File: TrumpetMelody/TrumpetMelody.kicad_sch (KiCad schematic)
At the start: 81 parts, among them J1 USB_B_Micro, J2 Conn_01x05, J3 640456-3, J4 640456-3, SW1 SW_Push, U1 STM32F411RETx, U2 TLV62565DBVR, U3 MAX98357AETE_T, U4 MAX7375AXR805

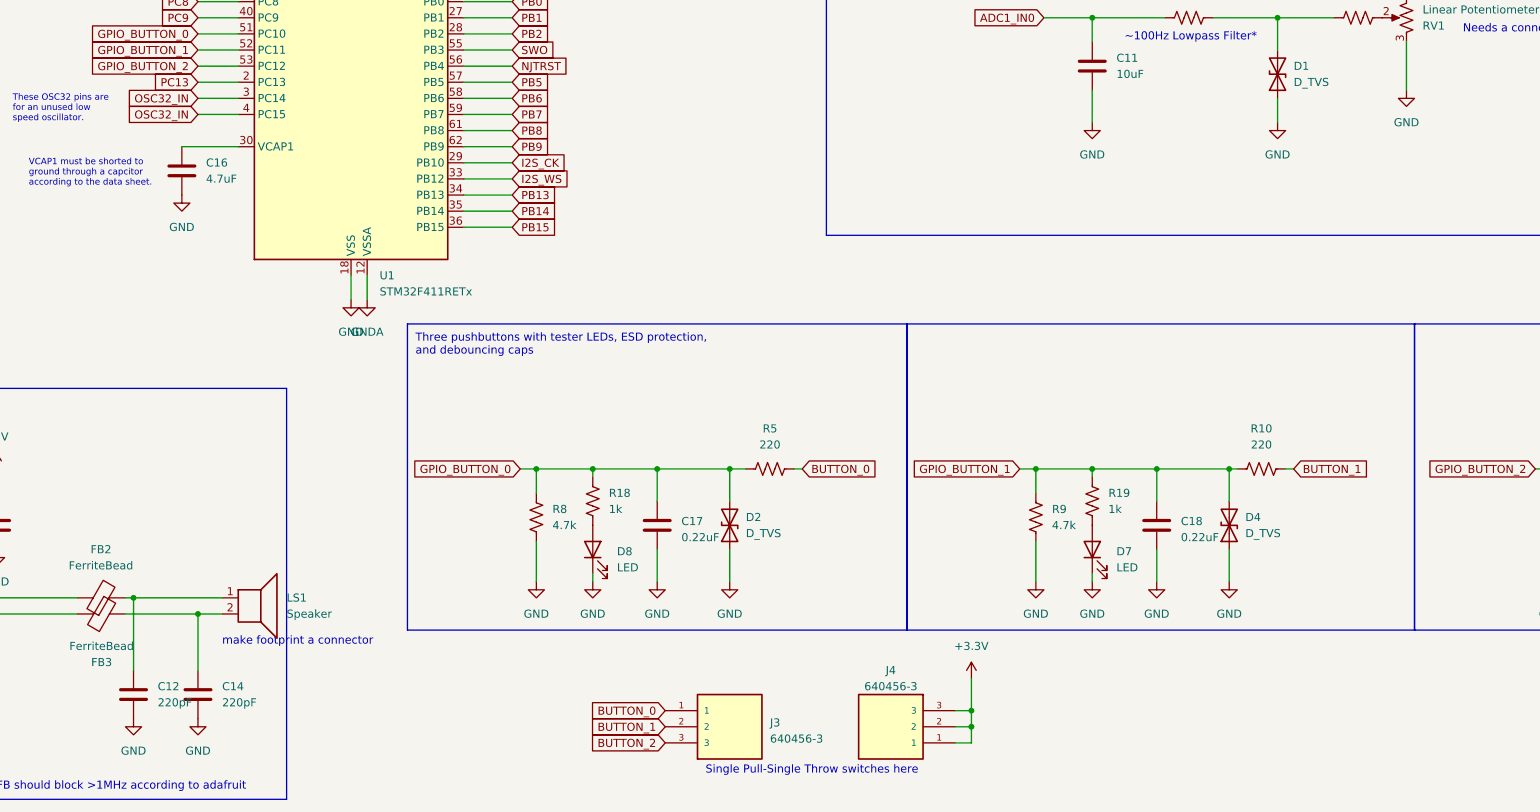
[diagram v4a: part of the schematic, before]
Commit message: Fixed grounds on the speaker and potentiometer
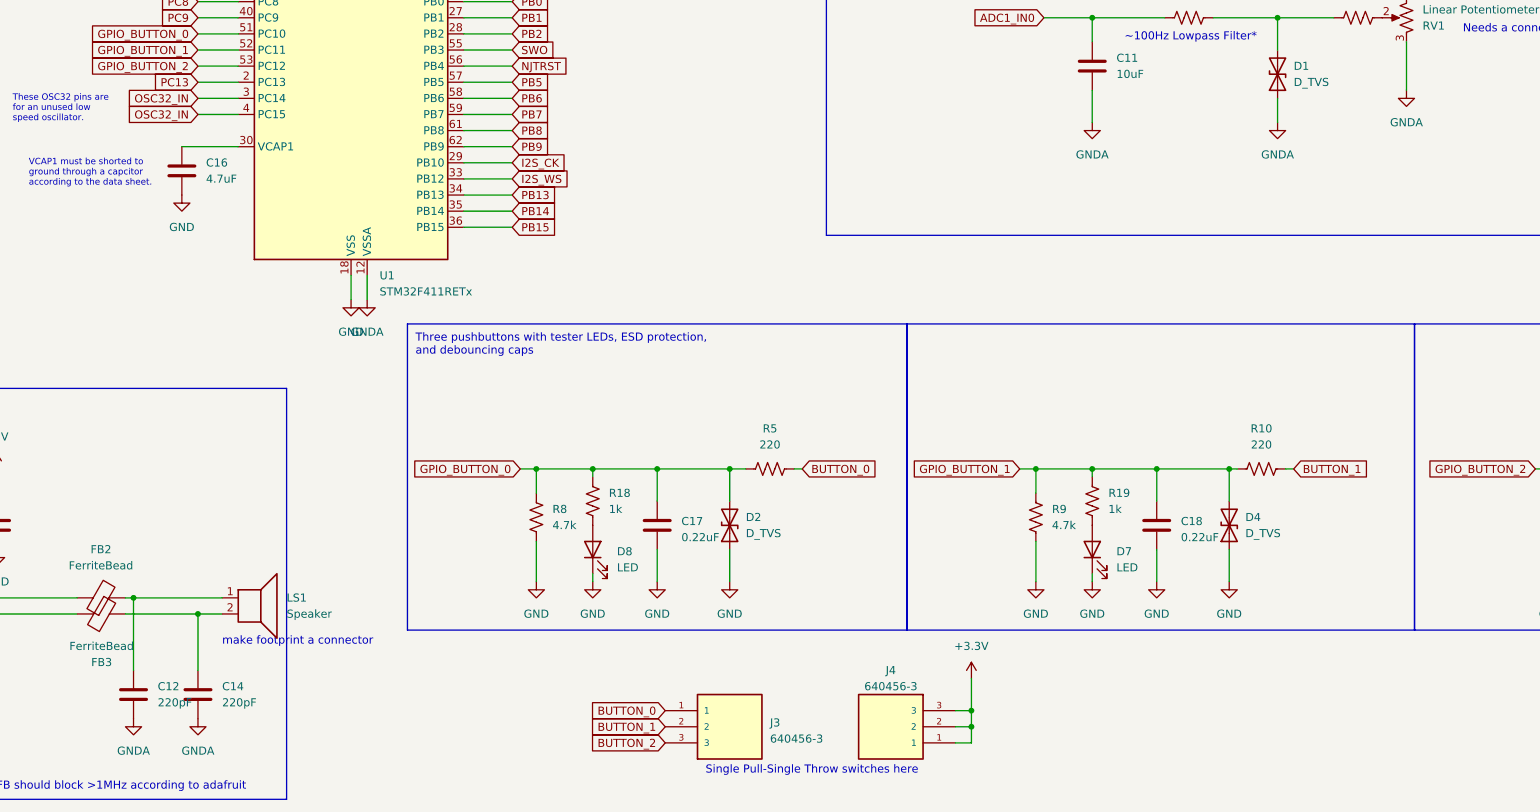
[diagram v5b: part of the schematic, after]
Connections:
- net GND: no longer C11.2, C12.2, C14.2, D1.1 (A1), RV1.3
- net GNDA: now also C11.2, C12.2, C14.2, D1.1 (A1), RV1.3
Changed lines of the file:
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@@
-    )
-  )
-  (symbol (lib_id "power:GND") (at 132.08 261.62 0) (unit 1)
-    (in_bom yes) (on_board yes) (dnp no) (fields_autoplaced)
-    (property "Reference" "#PWR037" (at 132.08 267.97 0)
-      (effects (font (size 1.27 1.27)) hide)
-    )
-    (property "Value" "GND" (at 132.08 266.7 0)
-      (effects (font (size 1.27 1.27)))
-    )
-    (property "Footprint" "" (at 132.08 261.62 0)
-      (effects (font (size 1.27 1.27)) hide)
-    )
-    (property "Datasheet" "" (at 132.08 261.62 0)
-      (effects (font (size 1.27 1.27)) hide)
-    )
-    (pin "1")
-    (instances
-      (project "TrumpetMelody"
-        (path "/646bb87a-580f-408c-a344-dec391089cbb"
-          (reference "#PWR037") (unit 1)
-        )
-      )
     )
   )
@@
     )
   )
+  (symbol (lib_id "power:GNDA") (at 322.58 162.56 0) (unit 1)
+    (in_bom yes) (on_board yes) (dnp no) (fields_autoplaced)
+    (property "Reference" "#PWR018" (at 322.58 168.91 0)
+      (effects (font (size 1.27 1.27)) hide)
+    )
+    (property "Value" "GNDA" (at 322.58 167.64 0)
+      (effects (font (size 1.27 1.27)))
+    )
+    (property "Footprint" "" (at 322.58 162.56 0)
+      (effects (font (size 1.27 1.27)) hide)
+    )
+    (property "Datasheet" "" (at 322.58 162.56 0)
+      (effects (font (size 1.27 1.27)) hide)
+    )
+    (pin "1")
+    (instances
+      (project "TrumpetMelody"
+        (path "/646bb87a-580f-408c-a344-dec391089cbb"
+          (reference "#PWR018") (unit 1)
+        )
+      )
+    )
+  )
   (symbol (lib_id "Device:R_US") (at 257.81 95.25 90) (unit 1)
     (in_bom yes) (on_board yes) (dnp no) (fields_autoplaced)
@@
     )
   )
+  (symbol (lib_id "power:GNDA") (at 121.92 261.62 0) (unit 1)
+    (in_bom yes) (on_board yes) (dnp no) (fields_autoplaced)
+    (property "Reference" "#PWR033" (at 121.92 267.97 0)
+      (effects (font (size 1.27 1.27)) hide)
+    )
+    (property "Value" "GNDA" (at 121.92 266.7 0)
+      (effects (font (size 1.27 1.27)))
+    )
+    (property "Footprint" "" (at 121.92 261.62 0)
+      (effects (font (size 1.27 1.27)) hide)
+    )
+    (property "Datasheet" "" (at 121.92 261.62 0)
+      (effects (font (size 1.27 1.27)) hide)
+    )
+    (pin "1")
+    (instances
+      (project "TrumpetMelody"
+        (path "/646bb87a-580f-408c-a344-dec391089cbb"
+          (reference "#PWR033") (unit 1)
+        )
+      )
+    )
+  )
+  (symbol (lib_id "power:GNDA") (at 302.26 167.64 0) (unit 1)
+    (in_bom yes) (on_board yes) (dnp no) (fields_autoplaced)
+    (property "Reference" "#PWR020" (at 302.26 173.99 0)
+      (effects (font (size 1.27 1.27)) hide)
+    )
+    (property "Value" "GNDA" (at 302.26 172.72 0)
+      (effects (font (size 1.27 1.27)))
+    )
+    (property "Footprint" "" (at 302.26 167.64 0)
+      (effects (font (size 1.27 1.27)) hide)
+    )
+    (property "Datasheet" "" (at 302.26 167.64 0)
+      (effects (font (size 1.27 1.27)) hide)
+    )
+    (pin "1")
+    (instances
+      (project "TrumpetMelody"
+        (path "/646bb87a-580f-408c-a344-dec391089cbb"
+          (reference "#PWR020") (unit 1)
+        )
+      )
+    )
+  )
   (symbol (lib_id "power:+5V") (at 15.24 20.32 0) (unit 1)
     (in_bom yes) (on_board yes) (dnp no) (fields_autoplaced)
@@
         (path "/646bb87a-580f-408c-a344-dec391089cbb"
           (reference "R6") (unit 1)
-        )
-      )
-    )
-  )
-  (symbol (lib_id "power:GND") (at 121.92 261.62 0) (unit 1)
-    (in_bom yes) (on_board yes) (dnp no) (fields_autoplaced)
-    (property "Reference" "#PWR036" (at 121.92 267.97 0)
-      (effects (font (size 1.27 1.27)) hide)
-    )
-    (property "Value" "GND" (at 121.92 266.7 0)
-      (effects (font (size 1.27 1.27)))
-    )
-    (property "Footprint" "" (at 121.92 261.62 0)
-      (effects (font (size 1.27 1.27)) hide)
-    )
-    (property "Datasheet" "" (at 121.92 261.62 0)
-      (effects (font (size 1.27 1.27)) hide)
-    )
-    (pin "1")
-    (instances
-      (project "TrumpetMelody"
-        (path "/646bb87a-580f-408c-a344-dec391089cbb"
-          (reference "#PWR036") (unit 1)
         )
       )
@@
         (path "/646bb87a-580f-408c-a344-dec391089cbb"
           (reference "RV1") (unit 1)
-        )
-      )
-    )
-  )
-  (symbol (lib_id "power:GND") (at 273.05 167.64 0) (unit 1)
-    (in_bom yes) (on_board yes) (dnp no) (fields_autoplaced)
-    (property "Reference" "#PWR021" (at 273.05 173.99 0)
-      (effects (font (size 1.27 1.27)) hide)
-    )
-    (property "Value" "GND" (at 273.05 172.72 0)
-      (effects (font (size 1.27 1.27)))
-    )
-    (property "Footprint" "" (at 273.05 167.64 0)
-      (effects (font (size 1.27 1.27)) hide)
-    )
-    (property "Datasheet" "" (at 273.05 167.64 0)
-      (effects (font (size 1.27 1.27)) hide)
-    )
-    (pin "1")
-    (instances
-      (project "TrumpetMelody"
-        (path "/646bb87a-580f-408c-a344-dec391089cbb"
-          (reference "#PWR021") (unit 1)
         )
       )
@@
     )
   )
-  (symbol (lib_id "power:GND") (at 322.58 162.56 0) (unit 1)
-    (in_bom yes) (on_board yes) (dnp no) (fields_autoplaced)
-    (property "Reference" "#PWR018" (at 322.58 168.91 0)
-      (effects (font (size 1.27 1.27)) hide)
-    )
-    (property "Value" "GND" (at 322.58 167.64 0)
-      (effects (font (size 1.27 1.27)))
-    )
-    (property "Footprint" "" (at 322.58 162.56 0)
-      (effects (font (size 1.27 1.27)) hide)
-    )
-    (property "Datasheet" "" (at 322.58 162.56 0)
-      (effects (font (size 1.27 1.27)) hide)
-    )
-    (pin "1")
-    (instances
-      (project "TrumpetMelody"
-        (path "/646bb87a-580f-408c-a344-dec391089cbb"
-          (reference "#PWR018") (unit 1)
-        )
-      )
-    )
-  )
   (symbol (lib_id "power:GND") (at 30.48 87.63 0) (unit 1)
     (in_bom yes) (on_board yes) (dnp no)
@@
     )
   )
+  (symbol (lib_id "power:GNDA") (at 273.05 167.64 0) (unit 1)
+    (in_bom yes) (on_board yes) (dnp no) (fields_autoplaced)
+    (property "Reference" "#PWR021" (at 273.05 173.99 0)
+      (effects (font (size 1.27 1.27)) hide)
+    )
+    (property "Value" "GNDA" (at 273.05 172.72 0)
+      (effects (font (size 1.27 1.27)))
+    )
+    (property "Footprint" "" (at 273.05 167.64 0)
+      (effects (font (size 1.27 1.27)) hide)
+    )
+    (property "Datasheet" "" (at 273.05 167.64 0)
+      (effects (font (size 1.27 1.27)) hide)
+    )
+    (pin "1")
+    (instances
+      (project "TrumpetMelody"
+        (path "/646bb87a-580f-408c-a344-dec391089cbb"
+          (reference "#PWR021") (unit 1)
+        )
+      )
+    )
+  )
   (symbol (lib_id "Device:C") (at 264.16 35.56 0) (unit 1)
     (in_bom yes) (on_board yes) (dnp no) (fields_autoplaced)
@@
     )
   )
-  (symbol (lib_id "power:GND") (at 302.26 167.64 0) (unit 1)
-    (in_bom yes) (on_board yes) (dnp no) (fields_autoplaced)
-    (property "Reference" "#PWR020" (at 302.26 173.99 0)
-      (effects (font (size 1.27 1.27)) hide)
-    )
-    (property "Value" "GND" (at 302.26 172.72 0)
-      (effects (font (size 1.27 1.27)))
-    )
-    (property "Footprint" "" (at 302.26 167.64 0)
-      (effects (font (size 1.27 1.27)) hide)
-    )
-    (property "Datasheet" "" (at 302.26 167.64 0)
-      (effects (font (size 1.27 1.27)) hide)
-    )
-    (pin "1")
-    (instances
-      (project "TrumpetMelody"
-        (path "/646bb87a-580f-408c-a344-dec391089cbb"
-          (reference "#PWR020") (unit 1)
-        )
-      )
+  (symbol (lib_id "power:GNDA") (at 132.08 261.62 0) (unit 1)
+    (in_bom yes) (on_board yes) (dnp no) (fields_autoplaced)
+    (property "Reference" "#PWR034" (at 132.08 267.97 0)
+      (effects (font (size 1.27 1.27)) hide)
+    )
+    (property "Value" "GNDA" (at 132.08 266.7 0)
+      (effects (font (size 1.27 1.27)))
+    )
+    (property "Footprint" "" (at 132.08 261.62 0)
+      (effects (font (size 1.27 1.27)) hide)
+    )
+    (property "Datasheet" "" (at 132.08 261.62 0)
+      (effects (font (size 1.27 1.27)) hide)
+    )
+    (pin "1")
+    (instances
+      (project "TrumpetMelody"
+        (path "/646bb87a-580f-408c-a344-dec391089cbb"
+          (reference "#PWR034") (unit 1)
+        )
+      )

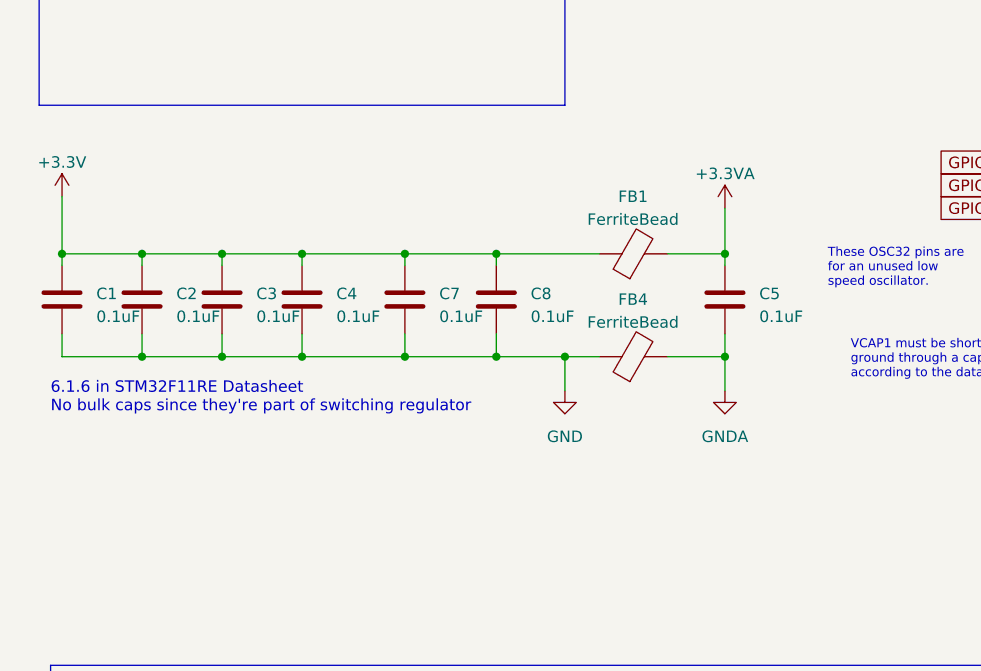
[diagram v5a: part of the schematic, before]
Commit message: Added decoupling caps to the micro
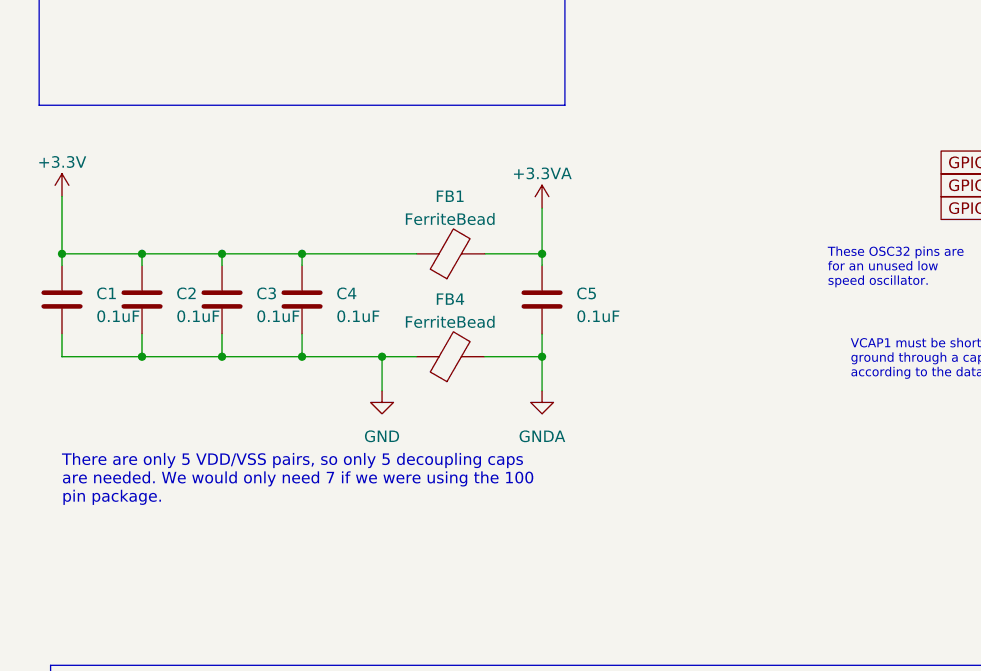
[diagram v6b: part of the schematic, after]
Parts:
- removed C7, C8: 0.1uF, Capacitor_SMD:C_0805_2012Metric_Pad1.18x1.45mm_HandSolder, symbol Device:C
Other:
- note added: "There are only 5 VDD/VSS pairs, so only 5 decoupling caps are needed. We would only need 7 if we were using the 100 pin package."
- note removed: "6.1.6 in STM32F11RE Datasheet No bulk caps since they're part of switching regulator"
- moved on the sheet: C5, FB1, FB4

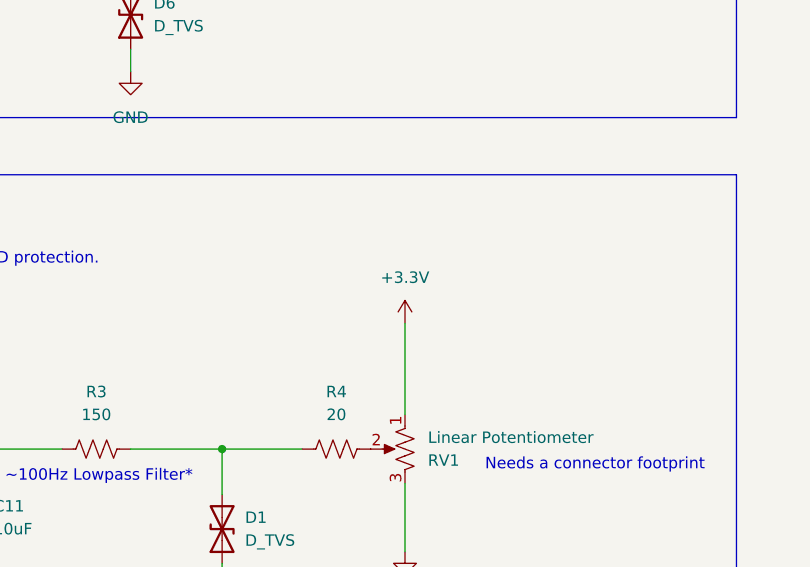
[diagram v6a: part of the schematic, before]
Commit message: Changed +3.3V on the poteniometer to +3.3VA
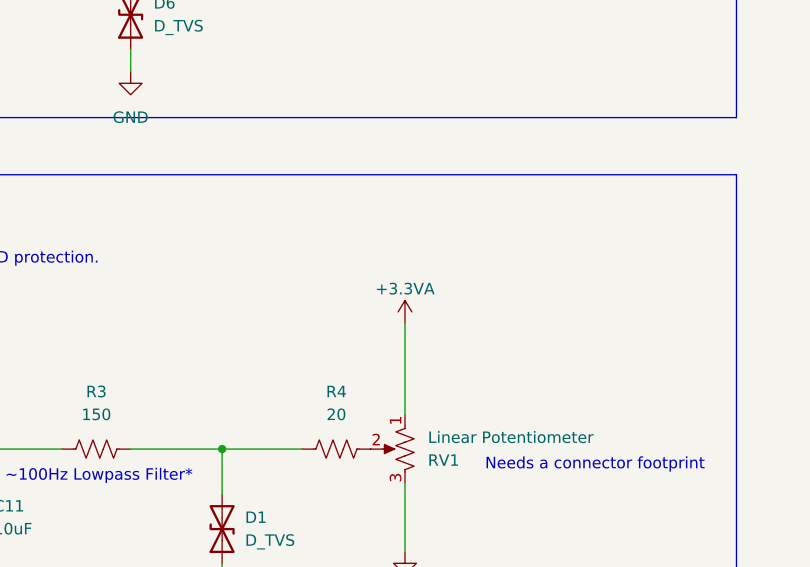
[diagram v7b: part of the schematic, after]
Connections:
- net +3.3V: no longer RV1.1
- net +3.3VA: now also RV1.1
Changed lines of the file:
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@@
-    )
-  )
-  (symbol (lib_id "power:+3.3V") (at 322.58 137.16 0) (unit 1)
-    (in_bom yes) (on_board yes) (dnp no) (fields_autoplaced)
-    (property "Reference" "#PWR019" (at 322.58 140.97 0)
-      (effects (font (size 1.27 1.27)) hide)
-    )
-    (property "Value" "+3.3V" (at 322.58 132.08 0)
-      (effects (font (size 1.27 1.27)))
-    )
-    (property "Footprint" "" (at 322.58 137.16 0)
-      (effects (font (size 1.27 1.27)) hide)
-    )
-    (property "Datasheet" "" (at 322.58 137.16 0)
-      (effects (font (size 1.27 1.27)) hide)
-    )
-    (pin "1")
-    (instances
-      (project "TrumpetMelody"
-        (path "/646bb87a-580f-408c-a344-dec391089cbb"
-          (reference "#PWR019") (unit 1)
-        )
-      )
     )
   )
@@
         )
       )
+    )
+  )
+  (symbol (lib_id "power:+3.3VA") (at 322.58 137.16 0) (unit 1)
+    (in_bom yes) (on_board yes) (dnp no) (fields_autoplaced)
+    (property "Reference" "#PWR019" (at 322.58 140.97 0)
+      (effects (font (size 1.27 1.27)) hide)
+    )
+    (property "Value" "+3.3VA" (at 322.58 133.35 0)
+      (effects (font (size 1.27 1.27)))
+    )
+    (property "Footprint" "" (at 322.58 137.16 0)
+      (effects (font (size 1.27 1.27)) hide)
+    )
+    (property "Datasheet" "" (at 322.58 137.16 0)
+      (effects (font (size 1.27 1.27)) hide)
+    )
+    (pin "1")
+    (instances
+      (project "TrumpetMelody"
+        (path "/646bb87a-580f-408c-a344-dec391089cbb"
+          (reference "#PWR019") (unit 1)
+        )
+      )
